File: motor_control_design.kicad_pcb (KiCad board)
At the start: 2 copper layers, 57.1 x 57.2 mm, 83 parts, among them J10 3V3, J2 SWD, J3 VBAT, J4 GND, J5 FC_M/P, J6 Conn_01x06, J8 Conn_01x06, J9 GND, Q1 RF1S9540SM, Q10 2N7002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

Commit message: intermediate
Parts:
- moved C10 1.31 mm to (152.0, 108.5)
- moved C9 0.85 mm to (150.0, 107.8)
- moved C3 0.49 mm to (153.0, 107.2)
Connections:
- J8 pad 7: +3.3V -> (no net)
- J8 pad 8: +3.3V -> (no net)
- U1 pad 11: unconnected-(U1-PA1-Pad11) -> /E2B
- U1 pad 15: /E2B -> unconnected-(U1-PA5-Pad15)
- U1 pad 17: unconnected-(U1-PA7-Pad17) -> /M1Q2
- U1 pad 33: /M1Q2 -> unconnected-(U1-PA12-Pad33)
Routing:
- net /E2B: track 8.04 -> 5.87 mm
- net GND: track 197.1 -> 198.8 mm
- net /NRST: track 42.3 -> 42.9 mm
- net (no net): vias 0 -> 1

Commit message: Routing, still messy
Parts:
- removed ? (x4): , 
- removed C14: 100uF, Capacitor_SMD:C_0805_2012Metric
- removed C15: 1000uF, Capacitor_SMD:CP_Elec_10x10.5
- removed D11: SS34, Diode_SMD:D_SMA
- removed L1: 100uH, Inductor_SMD:L_TaiTech_TMPC1265_13.5x12.5mm
- removed U3: LM2576S-3.3, Package_TO_SOT_SMD:TO-263-5_TabPin3
- added C12: .01uF, Capacitor_SMD:C_0402_1005Metric, F.Cu at (158.8, 91.4)
- added C13: 10uF, Capacitor_SMD:C_0402_1005Metric, F.Cu at (161.0, 94.5)
- added C16: 10uF, Capacitor_SMD:C_0402_1005Metric, F.Cu at (148.6, 65.0)
- added C17: 100nF, Capacitor_SMD:C_0402_1005Metric, F.Cu at (156.2, 70.9)
- added C18: 1uF, Capacitor_SMD:C_0402_1005Metric, F.Cu at (154.2, 75.4)
- added C19: 22uF, Capacitor_SMD:C_0402_1005Metric, F.Cu at (153.9, 76.7)
- added J1: TYPE-C-31-M-12, Connector_USB:USB_C_Receptacle_HRO_TYPE-C-31-M-12, F.Cu at (167.2, 109.5)
- added L2: 3.3uH, Inductor_SMD:L_0402_1005Metric, F.Cu at (152.7, 72.9)
- added R25: 5.11k, Resistor_SMD:R_0402_1005Metric, B.Cu at (168.4, 108.0)
- added R26: 5.11k, Resistor_SMD:R_0402_1005Metric, B.Cu at (164.8, 110.2)
- added R28: 56.2k, Resistor_SMD:R_0402_1005Metric, F.Cu at (155.2, 77.7)
- added R29: 10k, Resistor_SMD:R_0402_1005Metric, F.Cu at (156.2, 75.4)
- added U2: LT1962-3.3, Package_SO:MSOP-8_3x3mm_P0.65mm, F.Cu at (162.5, 92.0)
- added U4: TPS562200, Package_TO_SOT_SMD:SOT-23-6, F.Cu at (155.3, 73.2)
- moved J10 38.4 mm to (132.0, 104.5)
- moved J9 29.9 mm to (136.5, 108.0), turned to -54 degrees
- moved R1 2.74 mm to (139.4, 110.4), turned to -45 degrees
- moved D12 1.59 mm to (154.4, 102.4)
- moved C5 0.78 mm to (138.7, 104.8)
- moved D9 0.66 mm to (172.0, 102.5)
- moved Y1 0.56 mm to (141.2, 106.4)
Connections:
- J6 pad 4: +BATT -> +5V
- J8 pad 4: +BATT -> +5V
- J8 pad 7: (no net) -> +3.3V
- J8 pad 8: (no net) -> +3.3V
- Q10 pad 2: +3.3V -> GND
- Q11 pad 2: +3.3V -> GND
- Q12 pad 2: +3.3V -> GND
- Q8 pad 2: +3.3V -> GND
- R10 pad 1: GND -> +3.3V
- R21 pad 1: GND -> +3.3V
- R22 pad 1: GND -> +3.3V
- R9 pad 1: GND -> +3.3V
- U1 pad 15: unconnected-(U1-PA5-Pad15) -> /M1Q1
- U1 pad 32: /M1Q1 -> /USB_D-
- U1 pad 33: unconnected-(U1-PA12-Pad33) -> /USB_D+
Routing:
- net /USB_D-: track 0.00 -> 80.0 mm, vias 0 -> 2
- net +5V: track 0.00 -> 74.7 mm, vias 0 -> 3
- net /USB_D+: track 0.00 -> 71.9 mm, vias 0 -> 2
- net +BATT: track 231.4 -> 164.6 mm
- net /M1Q2: track 16.7 -> 78.1 mm, vias 1 -> 6
- net GND: track 198.8 -> 257.6 mm, vias 115 -> 71
- net Net-(D11-K): track 45.1 -> 0.00 mm
- net +3.3V: track 228.0 -> 186.6 mm, vias 9 -> 16
- net Net-(U4-SW): track 0.00 -> 5.96 mm
- net Net-(J1-CC2): track 0.00 -> 5.26 mm, vias 0 -> 1
- net Net-(J1-CC1): track 0.00 -> 5.24 mm, vias 0 -> 1
- net /E2B: track 5.87 -> 11.0 mm, vias 2 -> 3
- net /M1Q1: track 61.2 -> 65.4 mm, vias 2 -> 5
- net Net-(U4-VFB): track 0.00 -> 3.39 mm
- net /SWDIO: track 27.6 -> 30.9 mm
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- removed copper zone on B.Cu, net GND

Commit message: I think main routing done?
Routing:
- net /M1Q2: track 78.1 -> 77.4 mm
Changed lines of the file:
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@@
+	)
+	(segment
+		(start 154.15 101.541471)
+		(end 154.15 102.326911)
+		(width 0.2)
+		(layer "B.Cu")
+		(net 27)
+	)
+	(segment
+		(start 154.305 109.474)
+		(end 154.905 108.874)
+		(width 0.2)
+		(layer "B.Cu")
+		(net 27)
+	)
+	(segment
+		(start 159.258 108.204)
+		(end 159.258 102.785254)
+		(width 0.2)
+		(layer "B.Cu")
+		(net 27)
 	)
 	(segment
@@
 	)
 	(segment
-		(start 159.258 109.093)
-		(end 159.258 102.785254)
+		(start 154.564471 101.127)
+		(end 154.15 101.541471)
 		(width 0.2)
 		(layer "B.Cu")
@@
 	)
 	(segment
-		(start 157.599746 101.127)
-		(end 154.564471 101.127)
+		(start 139.685 95.108)
+		(end 139.065 94.488)
 		(width 0.2)
 		(layer "B.Cu")
@@
 	)
 	(segment
-		(start 139.685 95.108)
-		(end 139.065 94.488)
+		(start 138.071002 94.486001)
+		(end 135.786999 92.201998)
+		(width 0.2)
+		(layer "B.Cu")
+		(net 27)
+	)
+	(segment
+		(start 141.224 113.665)
+		(end 140.716 114.173)
 		(width 0.2)
 		(layer "B.Cu")
@@
 	)
 	(segment
-		(start 138.071002 94.486001)
-		(end 135.786999 92.201998)
+		(start 154.905 108.874)
+		(end 158.588 108.874)
 		(width 0.2)
 		(layer "B.Cu")
@@
 	)
 	(segment
-		(start 154.905 108.874)
-		(end 159.039 108.874)
-		(width 0.2)
-		(layer "B.Cu")
-		(net 27)
-	)
-	(segment
-		(start 141.224 113.665)
-		(end 140.716 114.173)
-		(width 0.2)
-		(layer "B.Cu")
-		(net 27)
-	)
-	(segment
-		(start 154.15 101.541471)
-		(end 154.15 102.326911)
+		(start 157.599746 101.127)
+		(end 154.564471 101.127)
 		(width 0.2)
 		(layer "B.Cu")
@@
 		(start 135.509 102.87)
 		(end 135.509 101.854)
-		(width 0.2)
-		(layer "B.Cu")
-		(net 27)
-	)
-	(segment
-		(start 159.039 108.874)
-		(end 159.258 109.093)
 		(width 0.2)
 		(layer "B.Cu")
@@
 	)
 	(segment
-		(start 154.564471 101.127)
-		(end 154.15 101.541471)
+		(start 158.588 108.874)
+		(end 159.258 108.204)
 		(width 0.2)
 		(layer "B.Cu")
-		(net 27)
-	)
-	(segment
-		(start 154.305 109.474)
-		(end 154.905 108.874)
-		(width 0.2)
-		(layer "B.Cu")

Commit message: Working through DRC
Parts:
- moved D5 0.94 mm to (126.2, 102.3)
- moved R1 0.73 mm to (138.8, 110.8)
- moved L2 0.10 mm to (152.6, 72.9)
- moved U2 0.07 mm to (162.4, 92.0)
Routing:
- net GND: track 257.6 -> 275.3 mm
- net +3.3V: track 186.6 -> 175.7 mm
- net /USB_D+: track 71.9 -> 75.5 mm
- net +BATT: track 164.6 -> 161.6 mm, vias 4 -> 2
- net +5V: track 74.7 -> 76.1 mm
- net /E2A: track 8.64 -> 9.57 mm
- net Net-(U4-VFB): track 3.39 -> 4.15 mm
- net /USB_D-: track 80.0 -> 80.6 mm
- net /M1Q2: track 77.4 -> 78.0 mm, vias 6 -> 5
- net Net-(Q14-G): track 32.7 -> 32.2 mm
- net /M1Q1: vias 5 -> 4
- added copper zone on B.Cu, net GND
- added copper zone on F.Cu, net GND

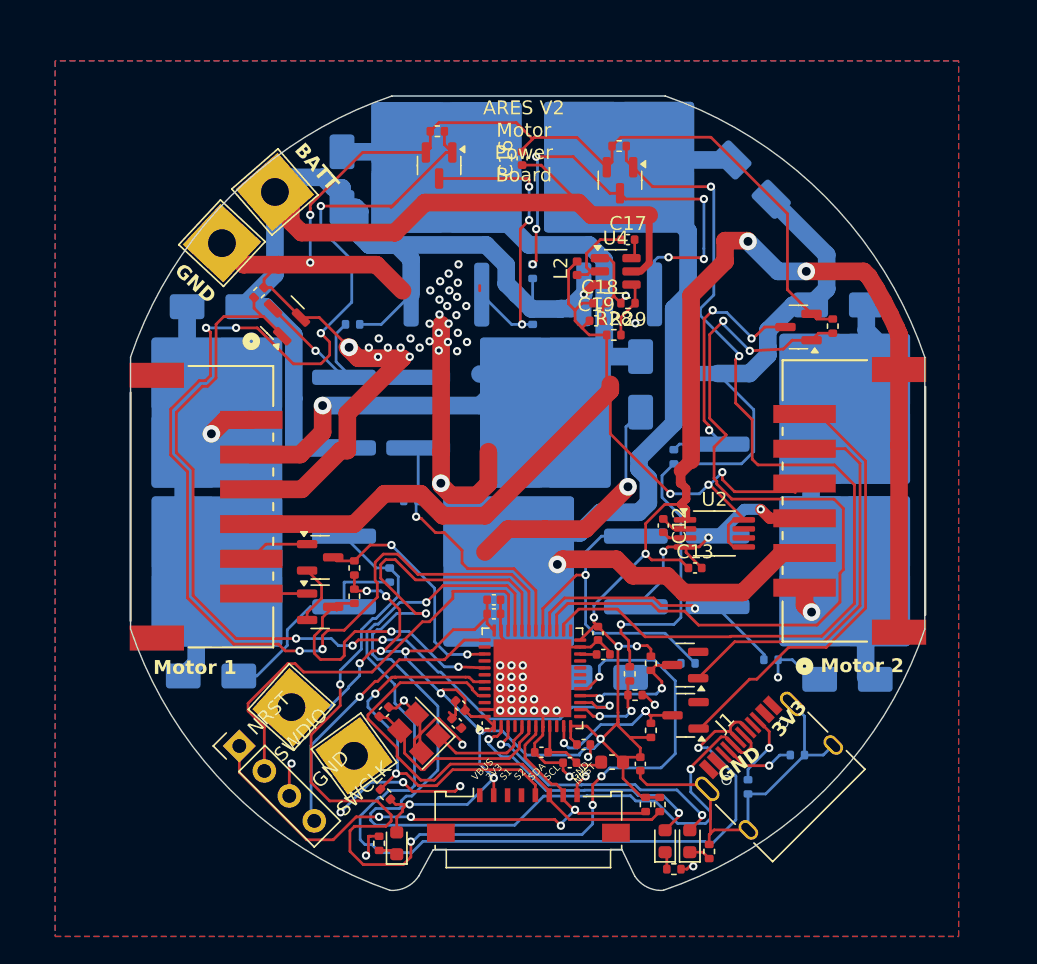
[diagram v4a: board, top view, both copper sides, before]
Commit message: added i2c, moved batt and ground pads back from edge
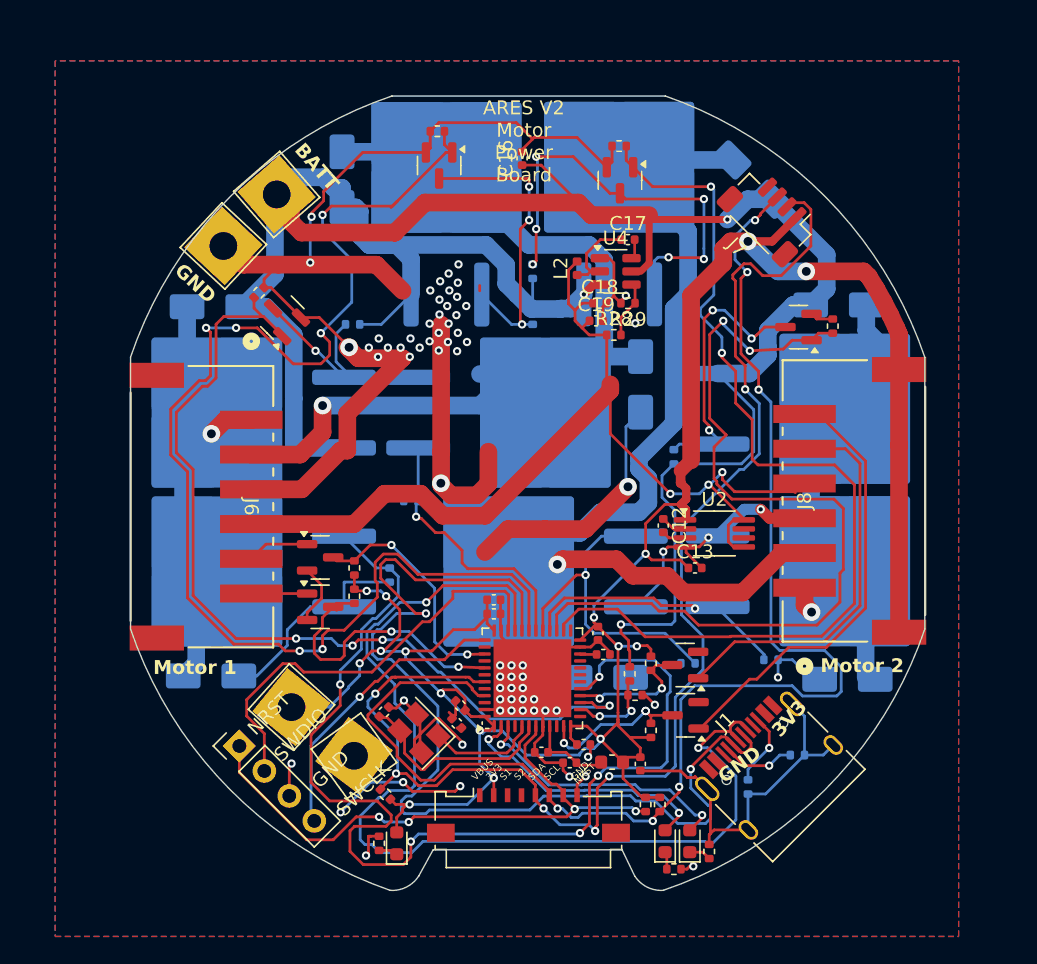
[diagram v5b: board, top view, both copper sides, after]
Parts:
- added J7: Conn_01x04_Pin, Connector_JST:JST_SH_BM04B-SRSS-TB_1x04-1MP_P1.00mm_Vertical, F.Cu at (166.4, 69.1)
- J10: value 3V3 -> 5V
- J6, J8: footprint JST-XH-SMD:CONN_S6B-XH-SM4-TB_JST -> Custom:CONN_S6B-XH-SM4-TB_JST
- moved J4 0.23 mm to (127.1, 71.3)
- moved J3 0.22 mm to (130.9, 67.6)
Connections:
- J10 pad 1: +3.3V -> +5V
- J8 pad 7: +3.3V -> (no net)
- J8 pad 8: +3.3V -> (no net)
- U1 pad 14: /VBatt_sense -> unconnected-(U1-PA4-Pad14)
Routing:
- net /SDA: track 29.1 -> 96.3 mm, vias 2 -> 6
- net /SCL: track 36.0 -> 100.0 mm, vias 0 -> 6
- net GND: track 275.3 -> 252.0 mm
- net +BATT: track 161.6 -> 170.7 mm, vias 2 -> 3
- net /USB_D-: track 80.6 -> 75.5 mm
- net +3.3V: track 175.7 -> 179.6 mm
- net /M1Q3: track 93.2 -> 92.7 mm

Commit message: working on DRC
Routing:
- net GND: track 252.0 -> 273.7 mm, vias 71 -> 76
- net /E2A: track 9.57 -> 9.01 mm

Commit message: TPS563200 Buck
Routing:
- net +3.3V: track 179.6 -> 134.6 mm, vias 16 -> 14
- net +5V: track 76.1 -> 102.4 mm, vias 3 -> 7
- net /USB_D-: track 75.5 -> 69.4 mm
- net /SWDIO: track 31.2 -> 30.4 mm
- net GND: track 273.7 -> 273.3 mm, vias 76 -> 110

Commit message: ADR1 layout changes
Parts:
- removed J8: Conn_01x06, Custom:CONN_S6B-XH-SM4-TB_JST
- removed L2: 3.3uH, Inductor_SMD:L_0402_1005Metric
- removed R29: 10k, Resistor_SMD:R_0402_1005Metric
- added C14: 10uF, Capacitor_SMD:C_0402_1005Metric, F.Cu at (161.3, 71.9)
- added C15: 10uF, Capacitor_SMD:C_0402_1005Metric, F.Cu at (161.3, 73.7)
- added L1: 3.3uH, Inductor_SMD:L_0402_1005Metric, F.Cu at (151.6, 72.9)
- added R27: 10k, Resistor_SMD:R_0402_1005Metric, F.Cu at (158.0, 74.6)
- C16: value 10uF -> 100nF
- C17: value 100nF -> 22uF
- U4: value TPS562200 -> TPS563200
- moved C16 10.9 mm to (157.8, 70.8), turned to 0 degrees
- moved R13 1.91 mm to (134.9, 75.7), turned to 90 degrees
- moved C11 0.80 mm to (157.7, 108.0)
- moved D7 0.74 mm to (135.0, 66.2)
- moved Q1 0.71 mm to (142.4, 67.3)
- moved D2 0.57 mm to (158.4, 114.4), turned to 0 degrees
- moved R19 0.48 mm to (166.3, 101.5)
- moved R20 0.47 mm to (149.3, 73.6)
- moved D9 0.42 mm to (172.2, 102.1)
- moved C17 0.33 mm to (155.9, 70.9)
- moved U4 0.28 mm to (155.0, 73.2)
- moved R16 0.26 mm to (138.8, 95.0)
- moved C4 0.13 mm to (144.2, 104.5)
- moved C1 0.12 mm to (146.4, 96.8)
- moved C8 0.12 mm to (146.4, 97.8)
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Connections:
- C16 pad 1: +BATT -> Net-(U4-SW)
- C16 pad 2: GND -> Net-(U4-VBST)
- C17 pad 1: Net-(U4-SW) -> +5V
- C17 pad 2: Net-(U4-VBST) -> GND
- J5 pad 1: VBUS -> +5V
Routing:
- net /M1Q3: track 92.7 -> 60.4 mm, vias 6 -> 2
- net GND: track 273.3 -> 248.4 mm, vias 110 -> 126
- net +5V: track 102.4 -> 114.6 mm, vias 7 -> 9
- net /SDA: track 96.3 -> 107.8 mm
- net /USB_D+: track 75.5 -> 65.5 mm, vias 2 -> 5
- net /M1Q1: track 65.4 -> 60.9 mm
- net /E1A: track 17.3 -> 21.7 mm
- net Net-(U4-SW): track 5.96 -> 9.32 mm, vias 0 -> 2
- net /SWDIO: track 30.4 -> 33.2 mm
- net +BATT: track 170.7 -> 168.1 mm, vias 3 -> 6
- net /SCL: track 100.0 -> 102.3 mm
- net Net-(Q14-G): track 32.2 -> 34.5 mm
- net +3.3V: track 134.6 -> 132.5 mm
- net Net-(J8-Pin_6): track 32.0 -> 33.8 mm
- net /OSC_IN: track 7.61 -> 9.18 mm
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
